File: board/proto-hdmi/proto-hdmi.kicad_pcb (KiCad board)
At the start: 2 copper layers, 30.5 x 43.2 mm, 48 parts, among them J1 Conn_02x17_Odd_Even, J2 HDMI_A, J3 HDMI_A, SW1 CTS_218-4LPSTR, U1 NTS0302, U2 NXP_NTS0302, U3 M24C02, U4 74LVC1G17

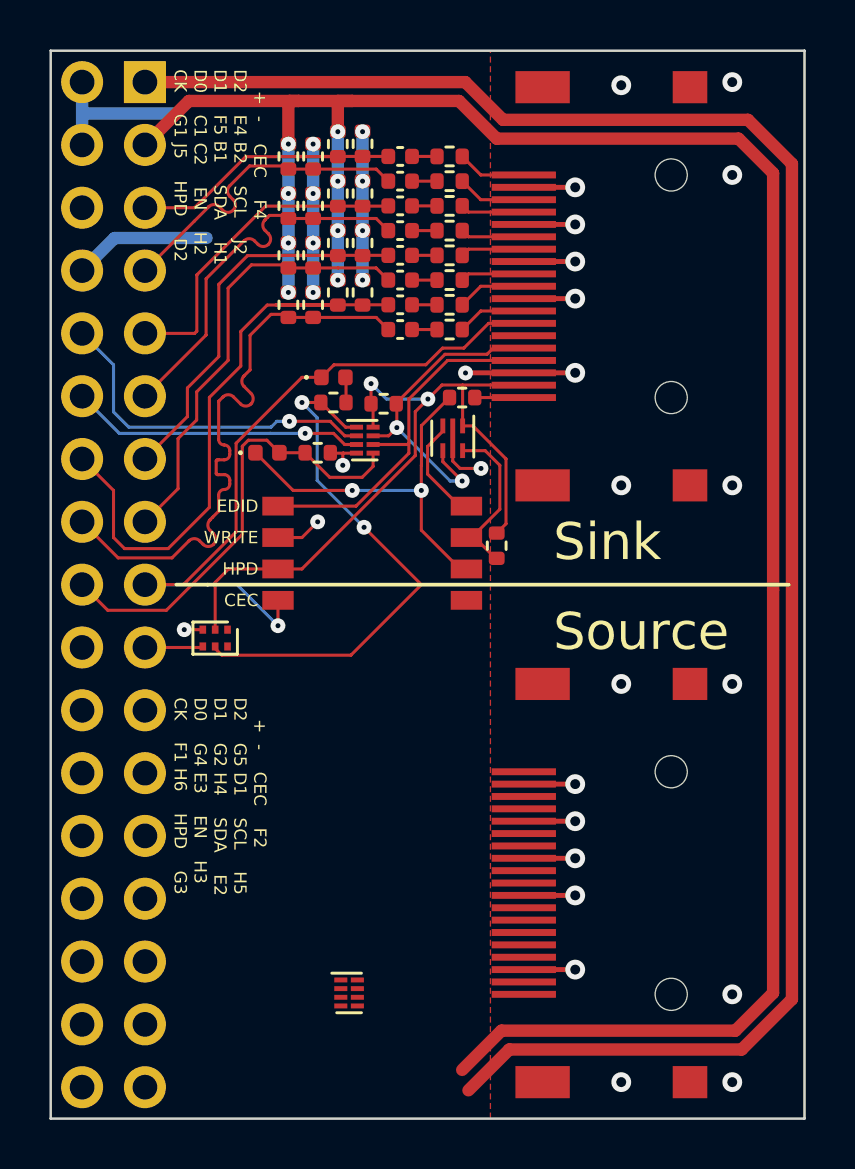
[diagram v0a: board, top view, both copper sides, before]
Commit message: Set up most of the non-TMDS source stuff.
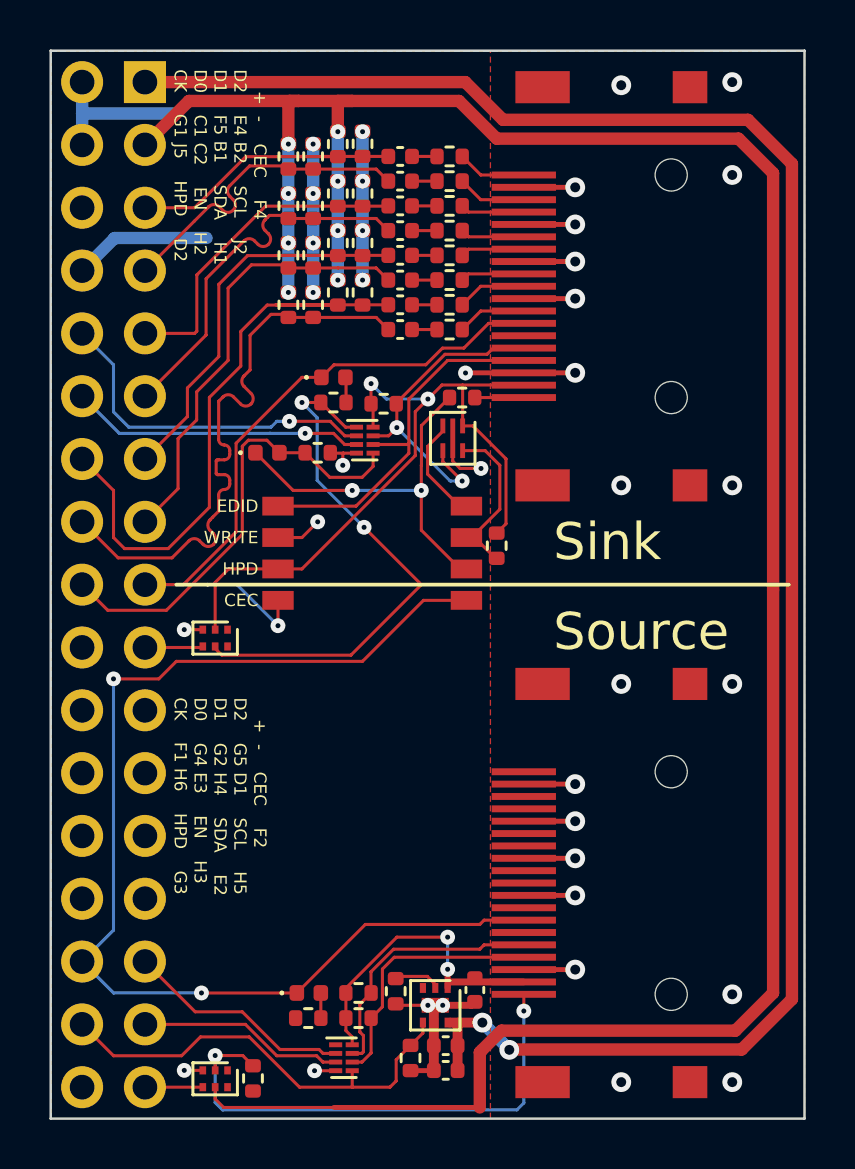
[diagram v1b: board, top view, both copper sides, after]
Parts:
- added C10: 1u, Capacitor_SMD:C_0402_1005Metric, F.Cu at (149.3, 130.4)
- added C11: 10u, Capacitor_SMD:C_0402_1005Metric, F.Cu at (150.5, 128.2)
- added C9: 22u, Capacitor_SMD:C_0402_1005Metric, F.Cu at (149.3, 131.4)
- added D3: SBA0520Q, Diode_SMD:D_0402_1005Metric, F.Cu at (143.8, 128.3)
- added R30: 412R, Resistor_SMD:R_0402_1005Metric, F.Cu at (147.3, 128.2)
- added R31: 2k, Resistor_SMD:R_0402_1005Metric, F.Cu at (145.8, 128.3)
- added R32: 2k, Resistor_SMD:R_0402_1005Metric, F.Cu at (145.8, 129.3)
- added R33: 47k, Resistor_SMD:R_0402_1005Metric, F.Cu at (141.5, 131.7)
- added R34: 27k, Resistor_SMD:R_0402_1005Metric, F.Cu at (143.8, 129.3)
- added R35: 10k, Resistor_SMD:R_0402_1005Metric, F.Cu at (147.9, 130.9)
- added U5: MIC2097-1, 0Local:Package_TMLF-6_EP_1.6mm, F.Cu at (148.9, 128.8)
- added U6: 74LVC1G17, Package_TO_SOT_SMD:SOT-886, F.Cu at (140.0, 131.7)
- moved U2 2.63 mm to (145.2, 130.9)
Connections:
- net VCC renamed +3V3
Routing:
- net /OUT_CEC: track 0.00 -> 47.1 mm, vias 0 -> 2
- net /HDMI Out/HDMI_HPD: track 0.00 -> 21.3 mm, vias 0 -> 2
- net /OUT_ENABLE: track 0.00 -> 18.0 mm
- net /HDMI Out/HDMI_+5V: track 0.00 -> 12.7 mm, vias 0 -> 2
- net +3V3: track 126.4 -> 138.9 mm
- net /HDMI Out/HDMI_SCL: track 0.00 -> 10.6 mm
- net /HDMI Out/HDMI_SDA: track 0.00 -> 10.4 mm
- net /OUT_SCL: track 0.00 -> 9.25 mm
- net GND: track 53.5 -> 61.9 mm, vias 33 -> 37
- net /OUT_SDA: track 0.00 -> 8.34 mm
- net +5V: track 75.9 -> 78.4 mm, vias 0 -> 2
- net /OUT_DETECT: track 0.00 -> 2.34 mm
- net Net-(R30-Pad1): track 0.00 -> 1.92 mm
- net Net-(D3-Pad2): track 0.00 -> 1.02 mm

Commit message: Add bonsai logo to boards.
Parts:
- added G***: LOGO, 0Local:Symbol_Bonsai_6.7mm, B.Cu at (151.1, 95.2)
- moved REF** 3.68 mm to (151.1, 101.6)

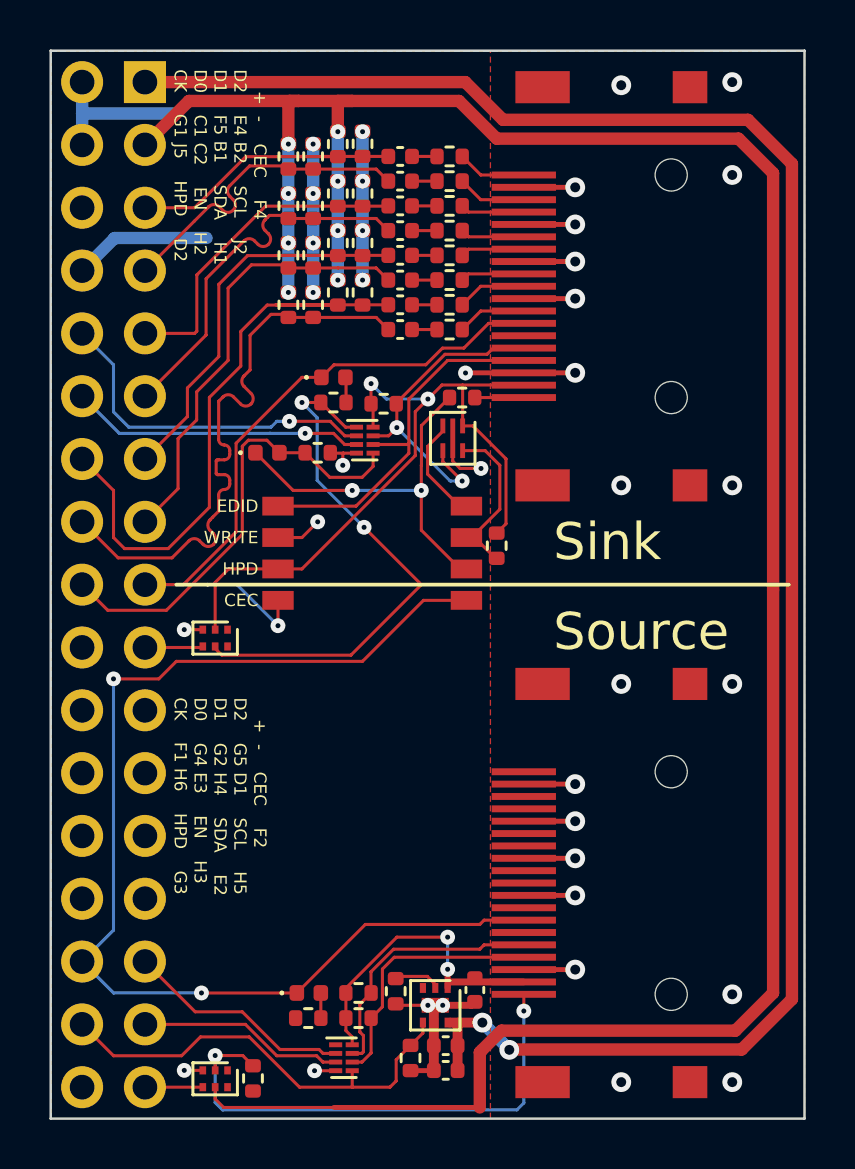
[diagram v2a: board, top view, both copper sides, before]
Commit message: Fix DRC issues on HDMI board.
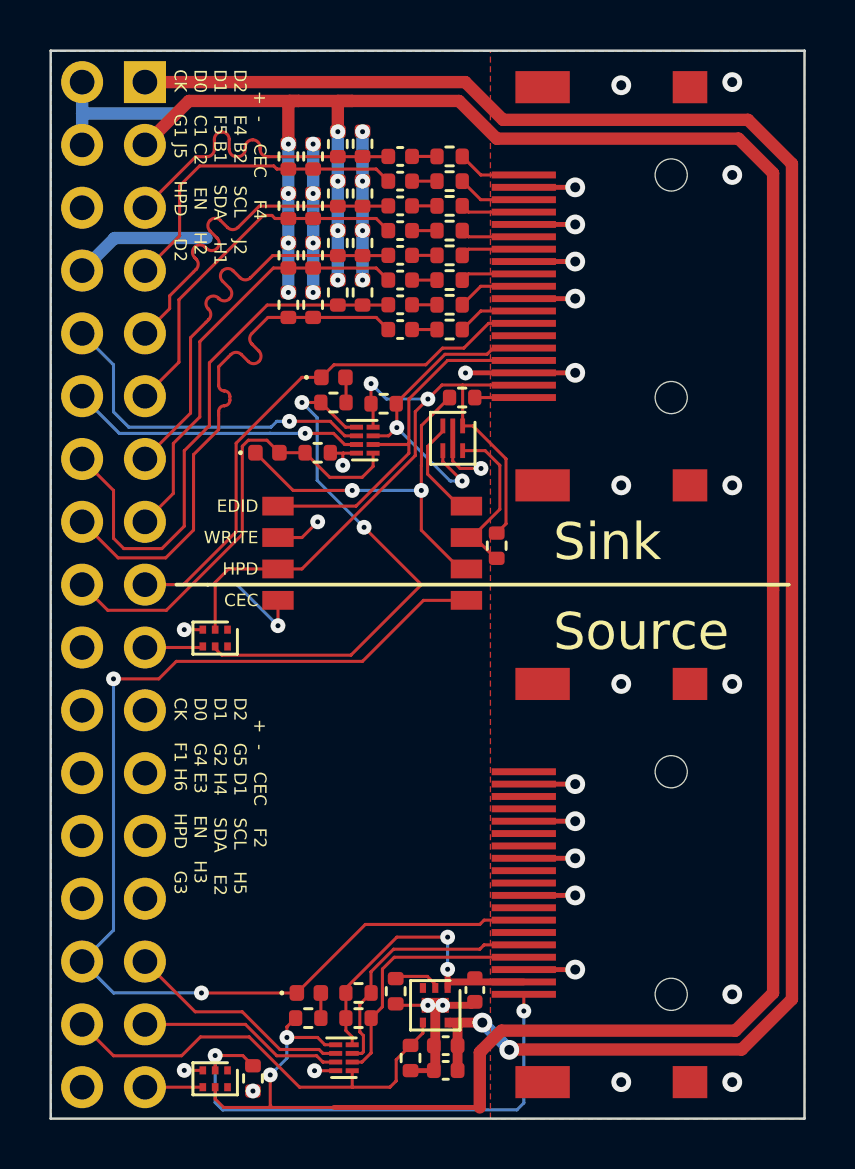
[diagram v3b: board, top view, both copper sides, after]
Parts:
- R30: value 412R -> 1k
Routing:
- net +3V3: track 138.9 -> 145.0 mm, vias 10 -> 12
- net /IN_CK_P: track 25.0 -> 22.4 mm
- net /IN_CK_N: track 24.5 -> 22.4 mm
- net /IN_D1_P: track 13.3 -> 14.5 mm
- net /IN_D0_P: track 18.1 -> 17.2 mm
- net /IN_D1_N: track 15.5 -> 14.6 mm
- net GND: track 61.9 -> 61.2 mm, vias 37 -> 38
- net /IN_D0_N: track 18.0 -> 17.3 mm

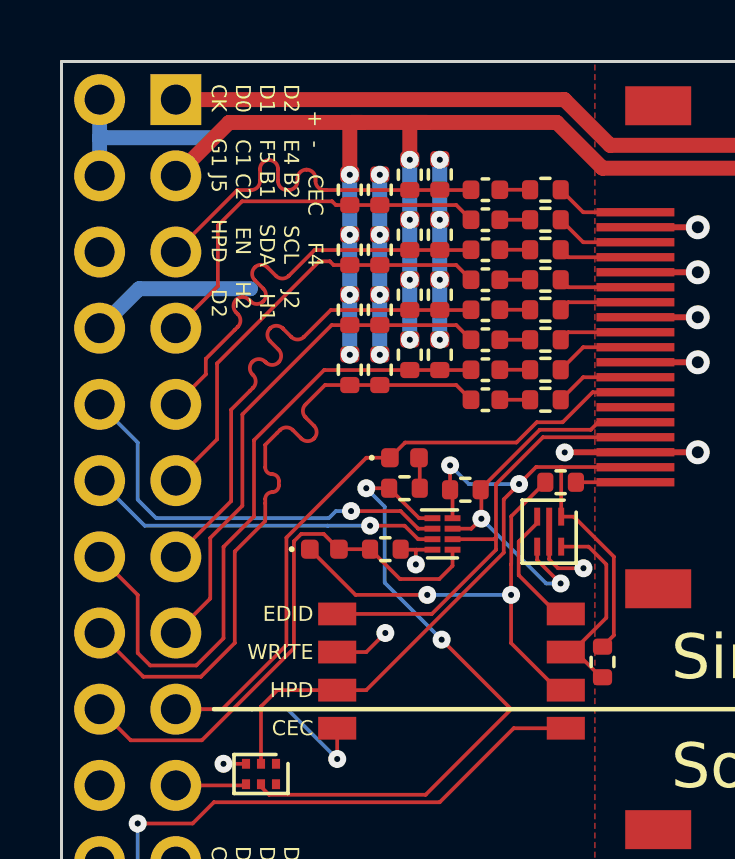
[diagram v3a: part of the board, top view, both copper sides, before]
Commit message: Deskew HDMI Proto sink lines.
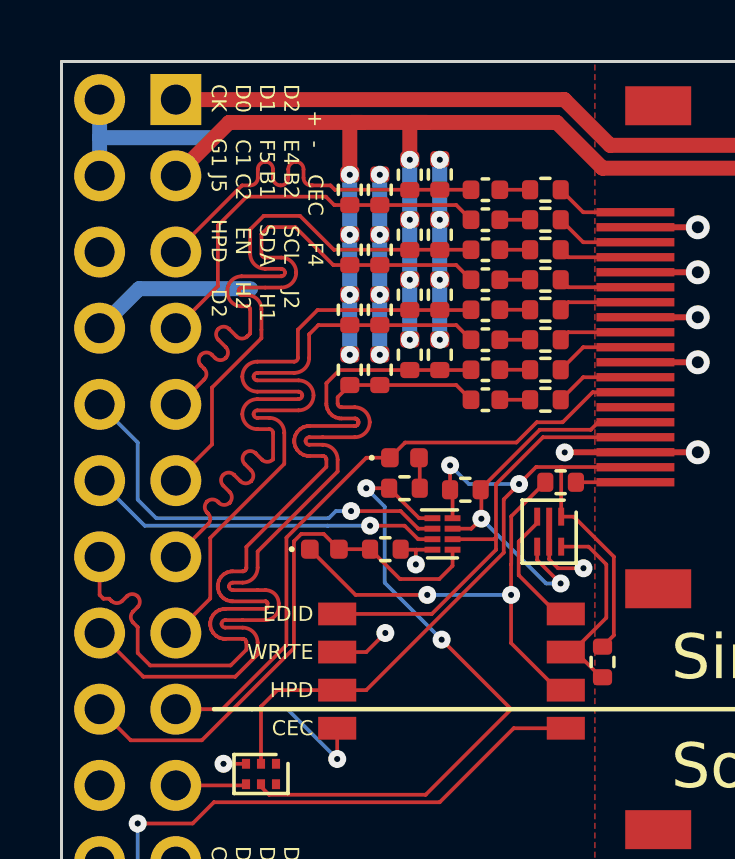
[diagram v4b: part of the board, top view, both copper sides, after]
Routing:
- net /IN_CK_P: track 22.4 -> 32.0 mm
- net /IN_D0_P: track 17.2 -> 23.5 mm
- net /IN_CK_N: track 22.4 -> 28.7 mm
- net /IN_D0_N: track 17.3 -> 22.9 mm
- net /IN_D1_N: track 14.6 -> 20.2 mm
- net /IN_D1_P: track 14.5 -> 20.0 mm

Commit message: Connect HDMI Proto output differential lines.
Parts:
- added C12: C, Capacitor_SMD:C_0402_1005Metric, F.Cu at (149.4, 118.6)
- added C13: C, Capacitor_SMD:C_0402_1005Metric, F.Cu at (149.4, 119.6)
- added C14: C, Capacitor_SMD:C_0402_1005Metric, F.Cu at (149.4, 120.7)
- added C15: C, Capacitor_SMD:C_0402_1005Metric, F.Cu at (149.4, 121.7)
- added C16: C, Capacitor_SMD:C_0402_1005Metric, F.Cu at (149.4, 122.7)
- added C17: C, Capacitor_SMD:C_0402_1005Metric, F.Cu at (149.4, 123.7)
- added C18: C, Capacitor_SMD:C_0402_1005Metric, F.Cu at (149.4, 124.7)
- added C19: C, Capacitor_SMD:C_0402_1005Metric, F.Cu at (149.4, 125.7)
- added R36: 82R, Resistor_SMD:R_0402_1005Metric, F.Cu at (147.8, 118.1)
- added R37: 82R, Resistor_SMD:R_0402_1005Metric, F.Cu at (147.8, 120.1)
- added R38: 82R, Resistor_SMD:R_0402_1005Metric, F.Cu at (147.8, 122.2)
- added R39: 82R, Resistor_SMD:R_0402_1005Metric, F.Cu at (146.8, 118.6)
- added R40: 82R, Resistor_SMD:R_0402_1005Metric, F.Cu at (146.8, 120.7)
- added R41: 82R, Resistor_SMD:R_0402_1005Metric, F.Cu at (146.8, 122.7)
- added R42: 82R, Resistor_SMD:R_0402_1005Metric, F.Cu at (147.8, 124.2)
- added R43: 82R, Resistor_SMD:R_0402_1005Metric, F.Cu at (146.8, 124.7)
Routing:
- net /OUT_D1_P: track 0.00 -> 27.2 mm
- net /OUT_D2_N: track 0.00 -> 25.3 mm
- net /OUT_D1_N: track 0.00 -> 25.1 mm
- net /OUT_D2_P: track 0.00 -> 21.3 mm
- net /OUT_CK_P: track 0.00 -> 20.2 mm
- net /OUT_D0_P: track 0.00 -> 17.8 mm
- net /OUT_D0_N: track 0.00 -> 17.0 mm
- net /OUT_CK_N: track 0.00 -> 15.4 mm
- net /HDMI Out/HDMI_CK_N: track 0.00 -> 2.99 mm
- net /HDMI Out/HDMI_CK_P: track 0.00 -> 2.99 mm
- net /HDMI Out/HDMI_D2_P: track 0.00 -> 2.91 mm
- net /HDMI Out/HDMI_D2_N: track 0.00 -> 2.91 mm
- net /HDMI Out/HDMI_D0_N: track 0.00 -> 2.77 mm
- net /HDMI Out/HDMI_D0_P: track 0.00 -> 2.77 mm
- net /HDMI Out/HDMI_D1_P: track 0.00 -> 2.69 mm
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
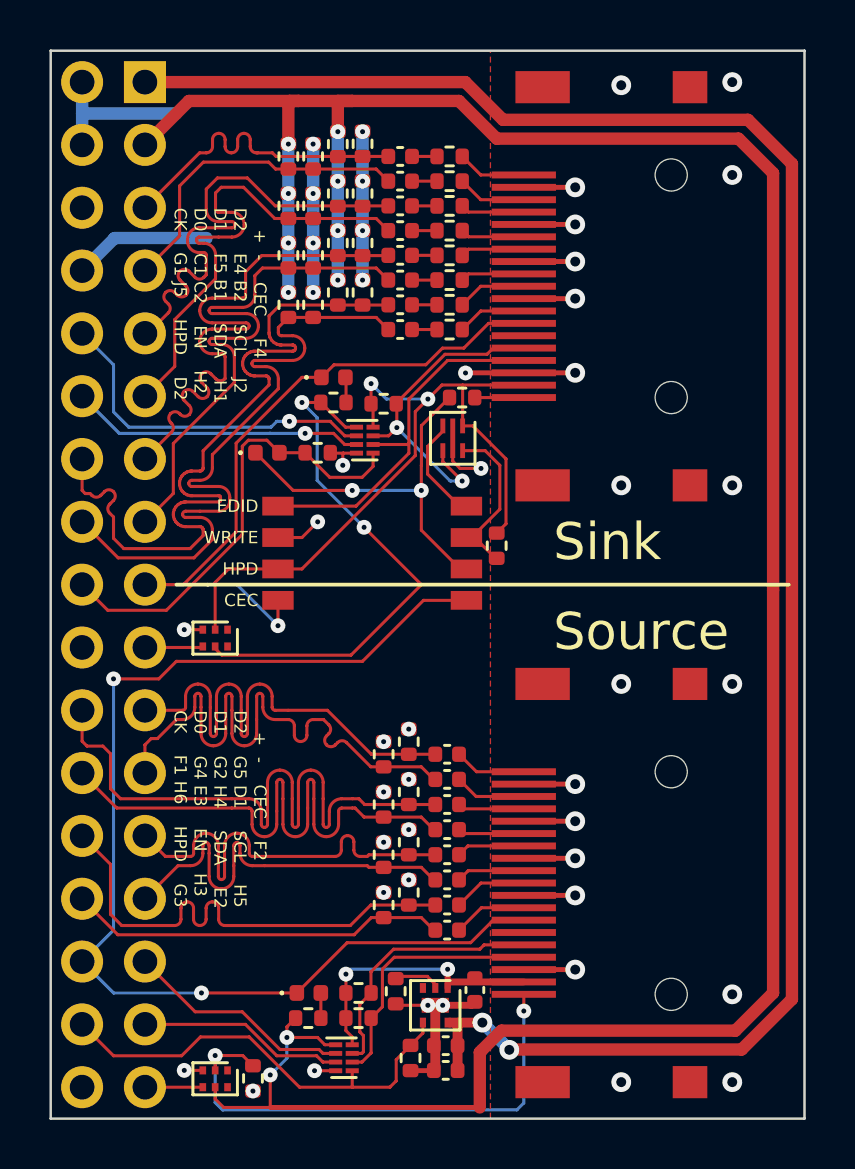
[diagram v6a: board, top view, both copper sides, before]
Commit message: Fix 1G17QDRY pinout.
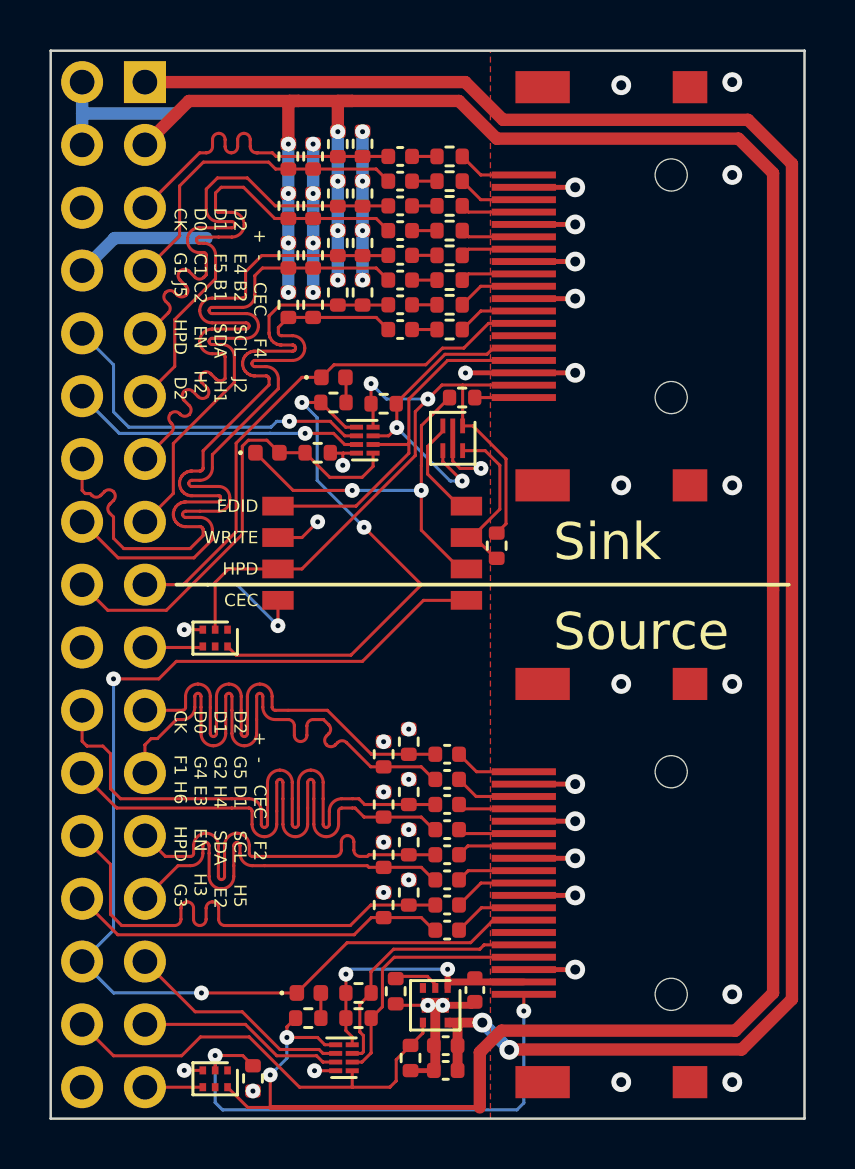
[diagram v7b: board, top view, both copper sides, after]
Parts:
- R1, R2, R3, R4, R5, R6, R7, R8: value 50R -> ${TMDS_R3}
- R10, R13, R14, R17, R18, R23, R24, R36, R37, R38, R39, R40, R41, R42, R43, R9: value 82R -> ${TMDS_R2}
- R11, R12, R15, R16, R19, R20, R25, R26: value 150R -> ${TMDS_R1}
- U1: value NTS0302 -> NXP_NTS0302
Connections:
- U4 pad 1: (no net) -> unconnected-(U4-Pad1)
- U4 pad 5: +3V3 -> unconnected-(U4-Pad5)
- U4 pad 6: (no net) -> +3V3
- U6 pad 1: (no net) -> unconnected-(U6-Pad1)
- U6 pad 5: +3V3 -> unconnected-(U6-Pad5)
- U6 pad 6: (no net) -> +3V3
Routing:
- net +3V3: track 145.1 -> 143.8 mm
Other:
- board text added: "for Olimex iCE40HX8K-EVB https://github.com/Elemecca/1240pi licensed under CERN-OHL-S v2"
- board text removed: "for Olimex iCE40HX8K-EVB https://github.com/Elemecca/1240pi licensed under CERN-OHL-P v2"
